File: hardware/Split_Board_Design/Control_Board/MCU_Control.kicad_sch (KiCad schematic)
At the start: 19 parts, among them J1 USB2.0_16P, Q3 BC817, Q4 BC817, SW1 ENABLE, U15 CH340C, U4 ESP32-WROOM-32E, U5 USBLC6-2SC6

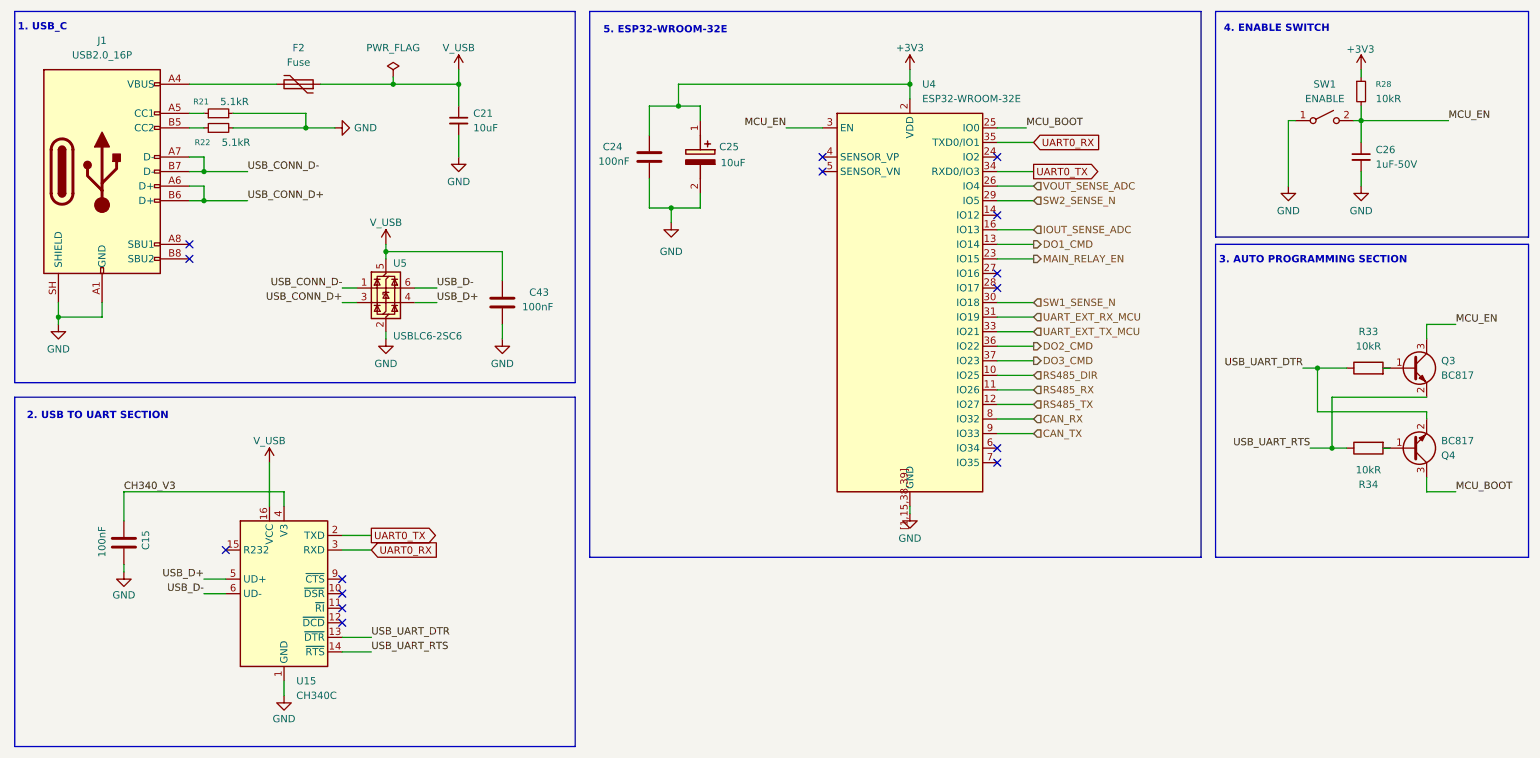
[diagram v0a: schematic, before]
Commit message: feat(layout): Finished demo schematic for control board
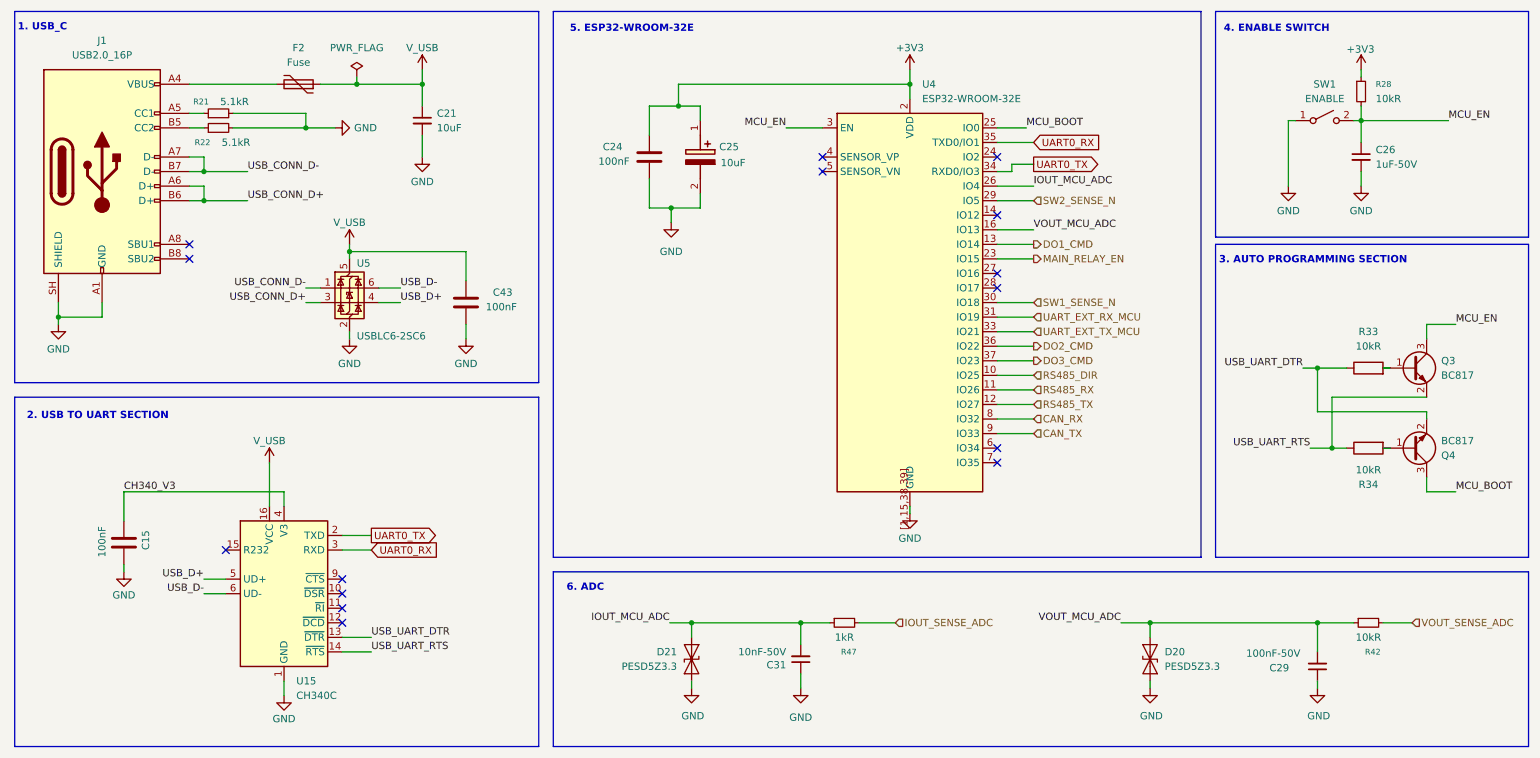
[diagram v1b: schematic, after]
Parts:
- added C29: 100nF-50V, Capacitor_SMD:C_0603_1608Metric, symbol Device:C_Small
- added C31: 10nF-50V, Capacitor_SMD:C_0603_1608Metric, symbol Device:C_Small
- added D20, D21: PESD5Z3.3, Diode_SMD:D_SOD-323, symbol Diode:ESD9B3.3ST5G
- added R42: 10kR, Resistor_SMD:R_0603_1608Metric, symbol Device:R_Small
- added R47: 1kR, Resistor_SMD:R_0603_1608Metric, symbol Device:R_Small
- C26: Link to Buy https://linhkien.cxtvn.com/11400-tu-105-1uf-0603-25v-10-20c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 -> https://linhkien.cxtvn.com/1982-tu-105-1uf-0603-50v-10-20c.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
- R33, R34: Link to Buy https://linhkien.cxtvn.com/9515-dien-tro-10k-0603-1-18w-50c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 -> https://linhkien.cxtvn.com/1422-dien-tro-10k-0603-1-100c.ht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
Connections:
- net GND: now also C29.1, C31.1, D20.2 (A2), D21.2 (A2)
- net IOUT_SENSE_ADC: now also R47.2; no longer U4.16 (IO13)
- net VOUT_SENSE_ADC: now also R42.2; no longer U4.26 (IO4)
- new net IOUT_MCU_ADC: C31.2, D21.1 (A1), R47.1, U4.26 (IO4)
- new net VOUT_MCU_ADC: C29.2, D20.1 (A1), R42.1, U4.16 (IO13)
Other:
- note added: "6. ADC"
- moved on the sheet: C21, C43, U5

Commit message: feat(layout): Update layout
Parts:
- C15, C24, C43: value 100nF -> 100nF-50V; footprint Capacitor_SMD:C_0805_2012Metric -> Capacitor_SMD:C_0603_1608Metric; Link to Buy https://linhkien.cxtvn.com/1976-tu-khong-phan-cuc-0805.html -> https://linhkien.cxtvn.com/1981-tu-0603-khong-phan-cuc.html
- C21: value 10uF -> 10uF-50V; footprint Capacitor_SMD:C_0805_2012Metric -> Capacitor_SMD:C_0603_1608Metric; Link to Buy https://linhkien.cxtvn.com/1976-tu-khong-phan-cuc-0805.html -> https://linhkien.cxtvn.com/2886-tu-106-10uf-0603-50v-10-20c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
- C25: value 10uF -> 10uF-25V
- C31: Link to Buy https://linhkien.cxtvn.com/6736-0603b104k500nt-tu-100nf-50v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 -> https://linhkien.cxtvn.com/2353-tu-103-10nf-0603-50v-10-20c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
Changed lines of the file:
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@@
 			)
 		)
-		(property "Link to Buy" "https://linhkien.cxtvn.com/6736-0603b104k500nt-tu-100nf-50v-10-0603-20c.html"
+		(property "Link to Buy" "https://linhkien.cxtvn.com/2353-tu-103-10nf-0603-50v-10-20c.html"
 			(at 66.04 260.35 0)
 			(hide yes)
@@
 			)
 		)
-		(property "Value" "10uF"
+		(property "Value" "10uF-25V"
 			(at 139.7 58.166 90)
 			(show_name no)
@@
 			)
 		)
-		(property "Value" "100nF"
+		(property "Value" "100nF-50V"
 			(at 31.75 127 90)
 			(show_name no)
@@
 			)
 		)
-		(property "Footprint" "Capacitor_SMD:C_0805_2012Metric"
+		(property "Footprint" "Capacitor_SMD:C_0603_1608Metric"
 			(at 36.5252 135.89 0)
 			(hide yes)
@@
 			)
 		)
-		(property "Link to Buy" "https://linhkien.cxtvn.com/1976-tu-khong-phan-cuc-0805.html"
+		(property "Link to Buy" "https://linhkien.cxtvn.com/1981-tu-0603-khong-phan-cuc.html"
 			(at -80.01 162.56 0)
 			(hide yes)
@@
 			)
 		)
-		(property "Value" "100nF"
+		(property "Value" "100nF-50V"
 			(at 118.364 57.912 0)
 			(show_name no)
@@
 			)
 		)
-		(property "Footprint" "Capacitor_SMD:C_0805_2012Metric"
+		(property "Footprint" "Capacitor_SMD:C_0603_1608Metric"
 			(at 128.2192 68.58 0)
 			(hide yes)
@@
 			)
 		)
-		(property "Link to Buy" "https://linhkien.cxtvn.com/1976-tu-khong-phan-cuc-0805.html"
+		(property "Link to Buy" "https://linhkien.cxtvn.com/1981-tu-0603-khong-phan-cuc.html"
 			(at 0 16.51 0)
 			(hide yes)
@@
 			)
 		)
-		(property "Value" "100nF"
+		(property "Value" "100nF-50V"
 			(at 104.14 83.312 0)
 			(show_name no)
@@
 			)
 		)
-		(property "Footprint" "Capacitor_SMD:C_0805_2012Metric"
+		(property "Footprint" "Capacitor_SMD:C_0603_1608Metric"
 			(at 94.2848 93.98 0)
 			(hide yes)
@@
 			)
 		)
-		(property "Link to Buy" "https://linhkien.cxtvn.com/1976-tu-khong-phan-cuc-0805.html"
+		(property "Link to Buy" "https://linhkien.cxtvn.com/1981-tu-0603-khong-phan-cuc.html"
 			(at 222.504 41.91 0)
 			(hide yes)
@@
 			)
 		)
-		(property "Value" "10uF"
+		(property "Value" "10uF-50V"
 			(at 90.17 52.0762 0)
 			(show_name no)
@@
 			)
 		)
-		(property "Footprint" "Capacitor_SMD:C_0805_2012Metric"
+		(property "Footprint" "Capacitor_SMD:C_0603_1608Metric"
 			(at 87.63 50.8 0)
 			(hide yes)
@@
 			)
 		)
-		(property "Link to Buy" "https://linhkien.cxtvn.com/1976-tu-khong-phan-cuc-0805.html"
+		(property "Link to Buy" "https://linhkien.cxtvn.com/2886-tu-106-10uf-0603-50v-10-20c.html"
 			(at 10.16 -17.78 0)
 			(hide yes)

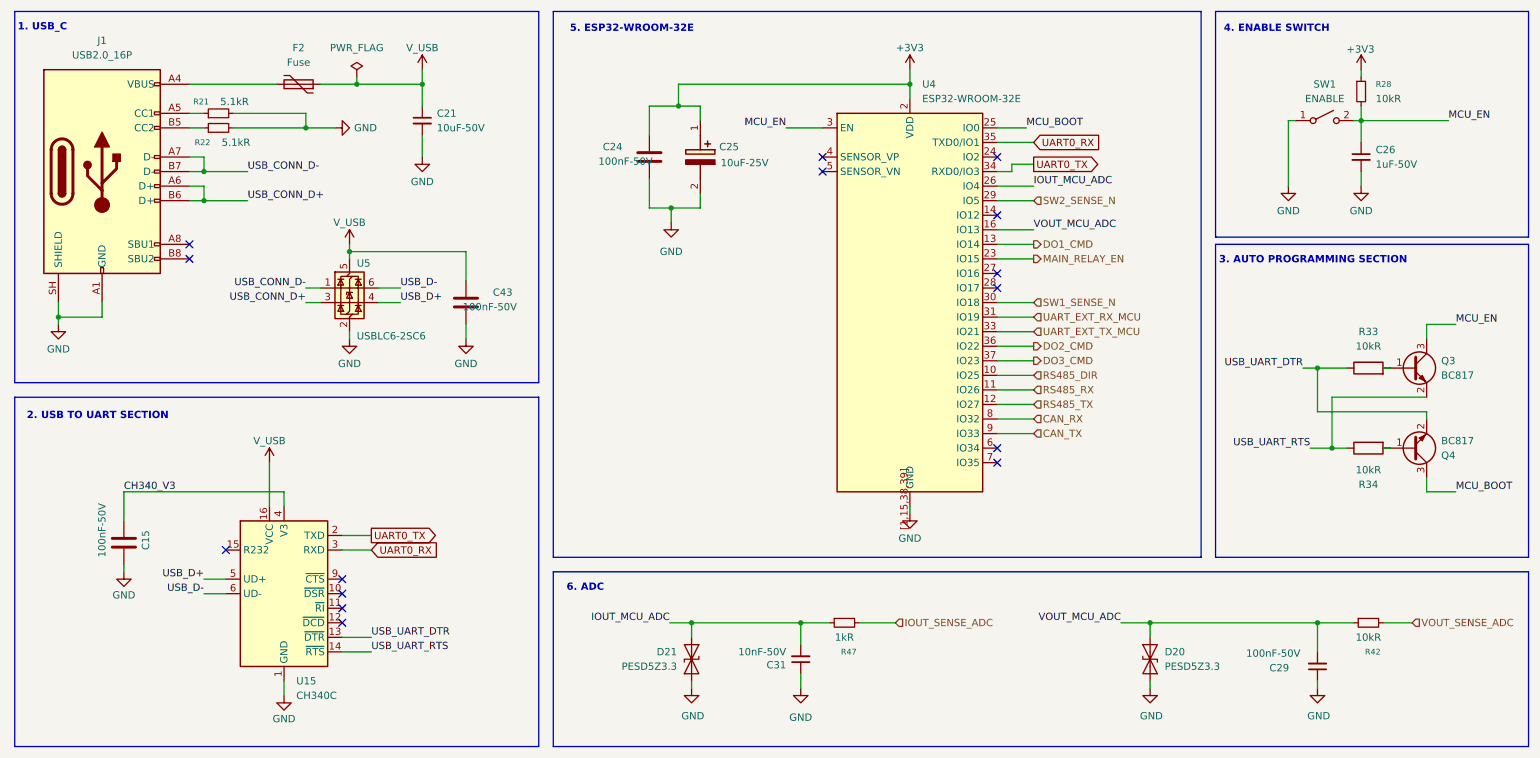
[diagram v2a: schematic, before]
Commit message: feat(schematic): update INA240A2PW to ÍNA240A2D
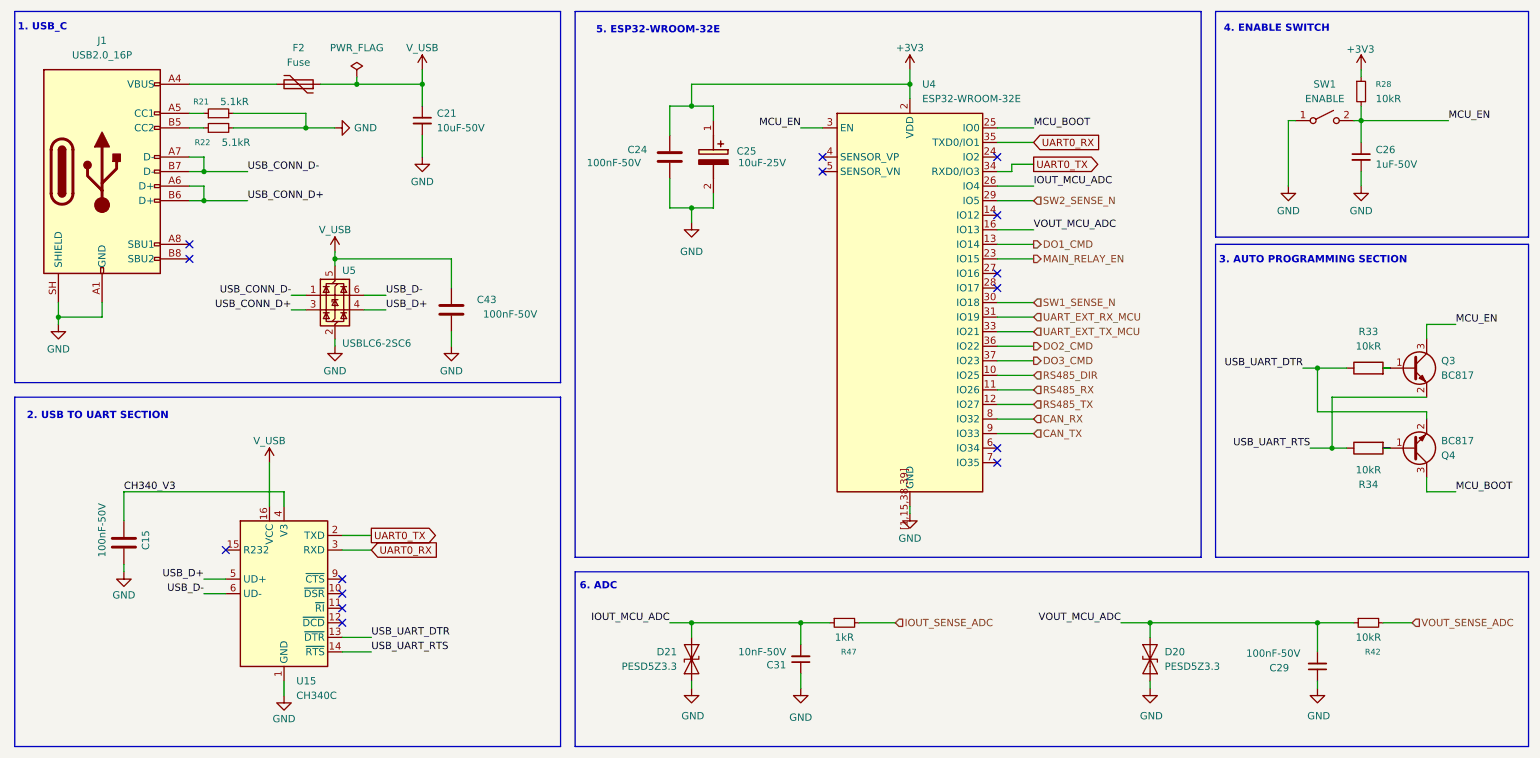
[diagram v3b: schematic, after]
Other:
- moved on the sheet: C24, C25, C43, U5

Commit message: Some minor updates
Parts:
- C31: value 10nF-50V -> 100nF-50V; Link to Buy https://linhkien.cxtvn.com/2353-tu-103-10nf-0603-50v-10-20c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 -> https://linhkien.cxtvn.com/1981-tu-0603-khong-phan-cuc.html
- R42: value 10kR -> 1kR
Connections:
- net IOUT_MCU_ADC: now also U4.6 (IO34); no longer U4.26 (IO4)
- net VOUT_MCU_ADC: now also U4.7 (IO35); no longer U4.16 (IO13)
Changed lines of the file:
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@@
 	)
 	(no_connect
+		(at 187.96 62.23)
+	)
+	(no_connect
 		(at 73.66 138.43)
 	)
@@
 	)
 	(no_connect
-		(at 187.96 107.95)
-	)
-	(no_connect
 		(at 157.48 57.15)
 	)
@@
 	)
 	(no_connect
-		(at 187.96 110.49)
+		(at 187.96 80.01)
 	)
 	(no_connect
-		(at 187.96 80.01)
+		(at 187.96 69.85)
 	)
 	(wire
@@
 	(wire
 		(pts
+			(xy 204.47 110.49) (xy 187.96 110.49)
+		)
+		(stroke
+			(width 0)
+			(type default)
+		)
+	)
+	(wire
+		(pts
 			(xy 130.81 66.04) (xy 134.62 66.04)
 		)
@@
 	(wire
 		(pts
-			(xy 187.96 62.23) (xy 194.31 62.23)
-		)
-		(stroke
-			(width 0)
-			(type default)
-		)
-	)
-	(wire
-		(pts
 			(xy 187.96 92.71) (xy 194.31 92.71)
 		)
@@
 	(wire
 		(pts
-			(xy 255.27 138.43) (xy 260.35 138.43)
+			(xy 187.96 107.95) (xy 204.47 107.95)
 		)
 		(stroke
@@
 	(wire
 		(pts
-			(xy 72.39 88.9) (xy 72.39 90.17)
+			(xy 255.27 138.43) (xy 260.35 138.43)
 		)
 		(stroke
@@
 	(wire
 		(pts
-			(xy 49.53 133.35) (xy 53.34 133.35)
+			(xy 72.39 88.9) (xy 72.39 90.17)
 		)
 		(stroke
@@
 	(wire
 		(pts
-			(xy 243.84 138.43) (xy 250.19 138.43)
+			(xy 49.53 133.35) (xy 53.34 133.35)
 		)
 		(stroke
@@
 	(wire
 		(pts
-			(xy 187.96 69.85) (xy 194.31 69.85)
+			(xy 243.84 138.43) (xy 250.19 138.43)
 		)
 		(stroke
@@
 		)
 	)
+	(label "IOUT_MCU_ADC"
+		(at 204.47 107.95 0)
+		(effects
+			(font
+				(size 1.27 1.27)
+			)
+			(justify left bottom)
+		)
+	)
 	(label "USB_D-"
 		(at 81.28 81.28 0)
@@
 		)
 	)
-	(label "CH340_V3"
-		(at 35.56 115.57 0)
+	(label "VOUT_MCU_ADC"
+		(at 204.47 110.49 0)
 		(effects
 			(font
@@
 		)
 	)
-	(label "IOUT_MCU_ADC"
-		(at 194.31 62.23 0)
+	(label "CH340_V3"
+		(at 35.56 115.57 0)
 		(effects
 			(font
@@
 		)
 	)
-	(label "VOUT_MCU_ADC"
-		(at 194.31 69.85 0)
-		(effects
-			(font
-				(size 1.27 1.27)
-			)
-			(justify left bottom)
-		)
-	)
 	(label "IOUT_MCU_ADC"
 		(at 130.81 138.43 180)
@@
 			)
 		)
-		(property "Value" "10nF-50V"
+		(property "Value" "100nF-50V"
 			(at 151.13 143.51 0)
 			(show_name no)
@@
 			)
 		)
-		(property "Link to Buy" "https://linhkien.cxtvn.com/2353-tu-103-10nf-0603-50v-10-20c.html"
+		(property "Link to Buy" "https://linhkien.cxtvn.com/1981-tu-0603-khong-phan-cuc.html"
 			(at 66.04 260.35 0)
 			(hide yes)
@@
 			)
 		)
-		(property "Value" "10kR"
+		(property "Value" "1kR"
 			(at 252.73 140.97 90)
 			(show_name no)

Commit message: feat(layout): update control board layout
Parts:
- removed C43: 100nF-50V, Capacitor_SMD:C_0603_1608Metric, symbol Device:C
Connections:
- net DO2_CMD: now also U4.16 (IO13); no longer U4.36 (IO22)
- net DO3_CMD: now also U4.24 (IO2); no longer U4.37 (IO23)
- net IOUT_MCU_ADC: no longer D21.1 (A1)
- net IOUT_SENSE_ADC: now also D21.1 (A1)
- net UART_EXT_RX_MCU: now also U4.33 (IO21); no longer U4.31 (IO19)
- net UART_EXT_TX_MCU: now also U4.31 (IO19); no longer U4.33 (IO21)
- net VOUT_MCU_ADC: no longer D20.1 (A1)
- net VOUT_SENSE_ADC: now also D20.1 (A1)
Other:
- moved on the sheet: C29, C31, D20, D21, F2, R42, R47

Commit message: layout: update layout
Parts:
- added C22: 10uF-50V, Capacitor_SMD:C_0603_1608Metric, symbol Device:C_Small
- D20: footprint Diode_SMD:D_SOD-323 -> Diode_SMD:D_SOD-523; LCSC Part C96512 -> (none); Link to Buy https://linhkienthuduc.com/san-pham/pesd5z3-3/ -> (none); MPN PESD5Z3.3 -> (none); Manufacturer Nexperia -> (none)
- D21: footprint Diode_SMD:D_SOD-323 -> Diode_SMD:D_SOD-523; LCSC Part C96512 -> (none); Link to Buy https://linhkienthuduc.com/san-pham/pesd5z3-3/ -> https://linhkien.cxtvn.com/7411-pesd5z33-tvs-diode-33vwm-18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; Manufacturer Nexperia -> (none)
- Q3, Q4: footprint Package_TO_SOT_SMD:SOT-23 -> Package_TO_SOT_SMD:SOT-23-3
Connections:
- net +3V3: now also U15.16 (VCC), C22.1
- net GND: now also C22.2
- net V_USB: no longer U15.16 (VCC)
